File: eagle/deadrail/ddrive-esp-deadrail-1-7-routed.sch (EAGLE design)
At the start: 20 parts, among them Q1 BSS123, Q2 BSS123, Q3 BSS123, Q4 BSS123

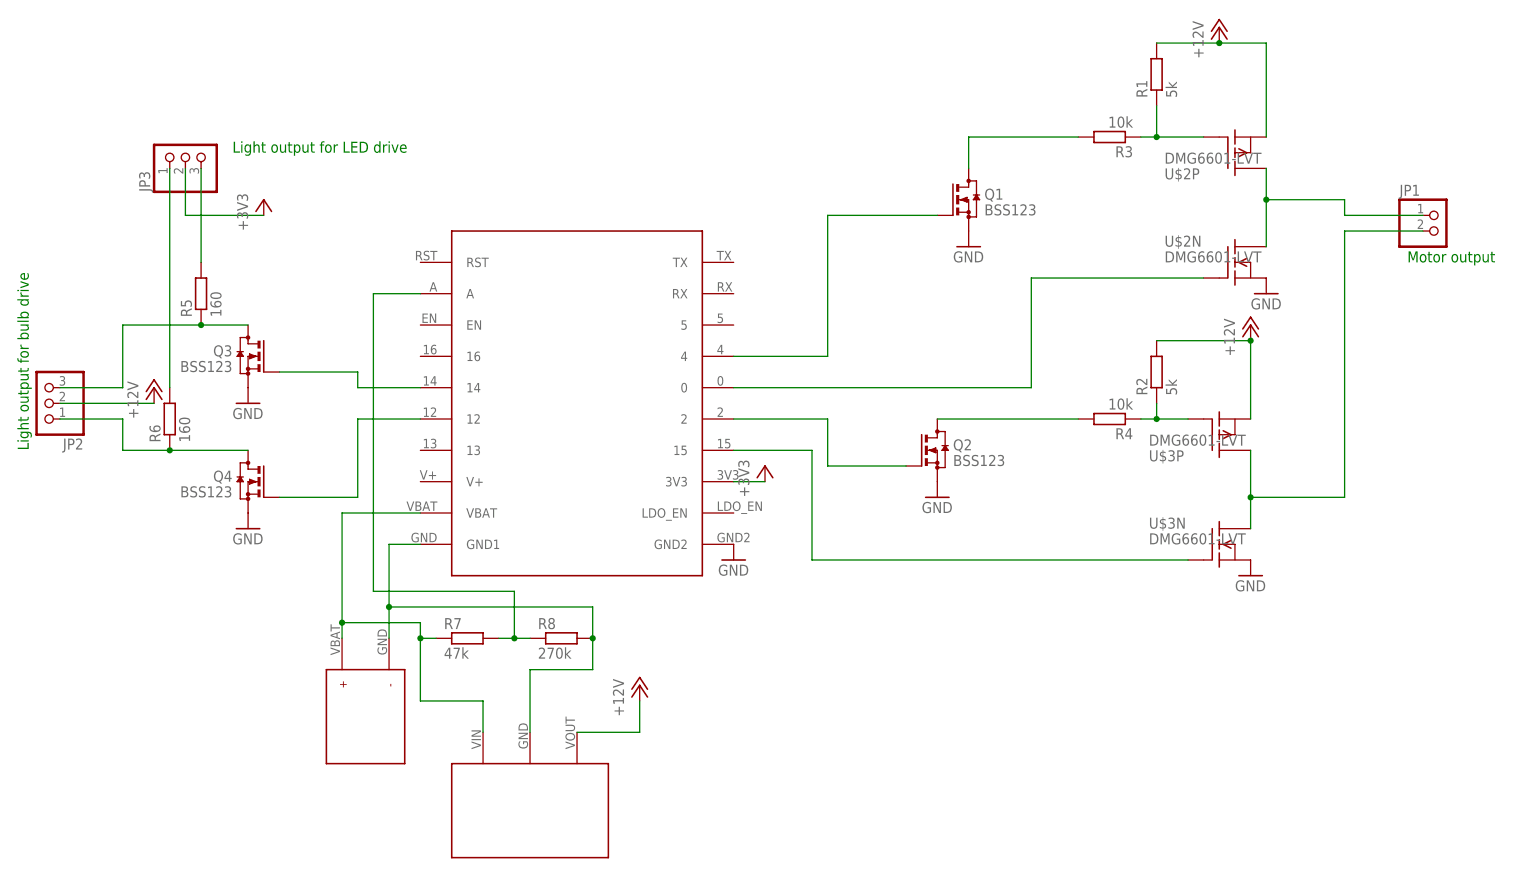
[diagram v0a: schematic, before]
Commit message: Adds all intermediate and the final schematic and board layout for the huzzah baseboard for esp-12 train decoder.
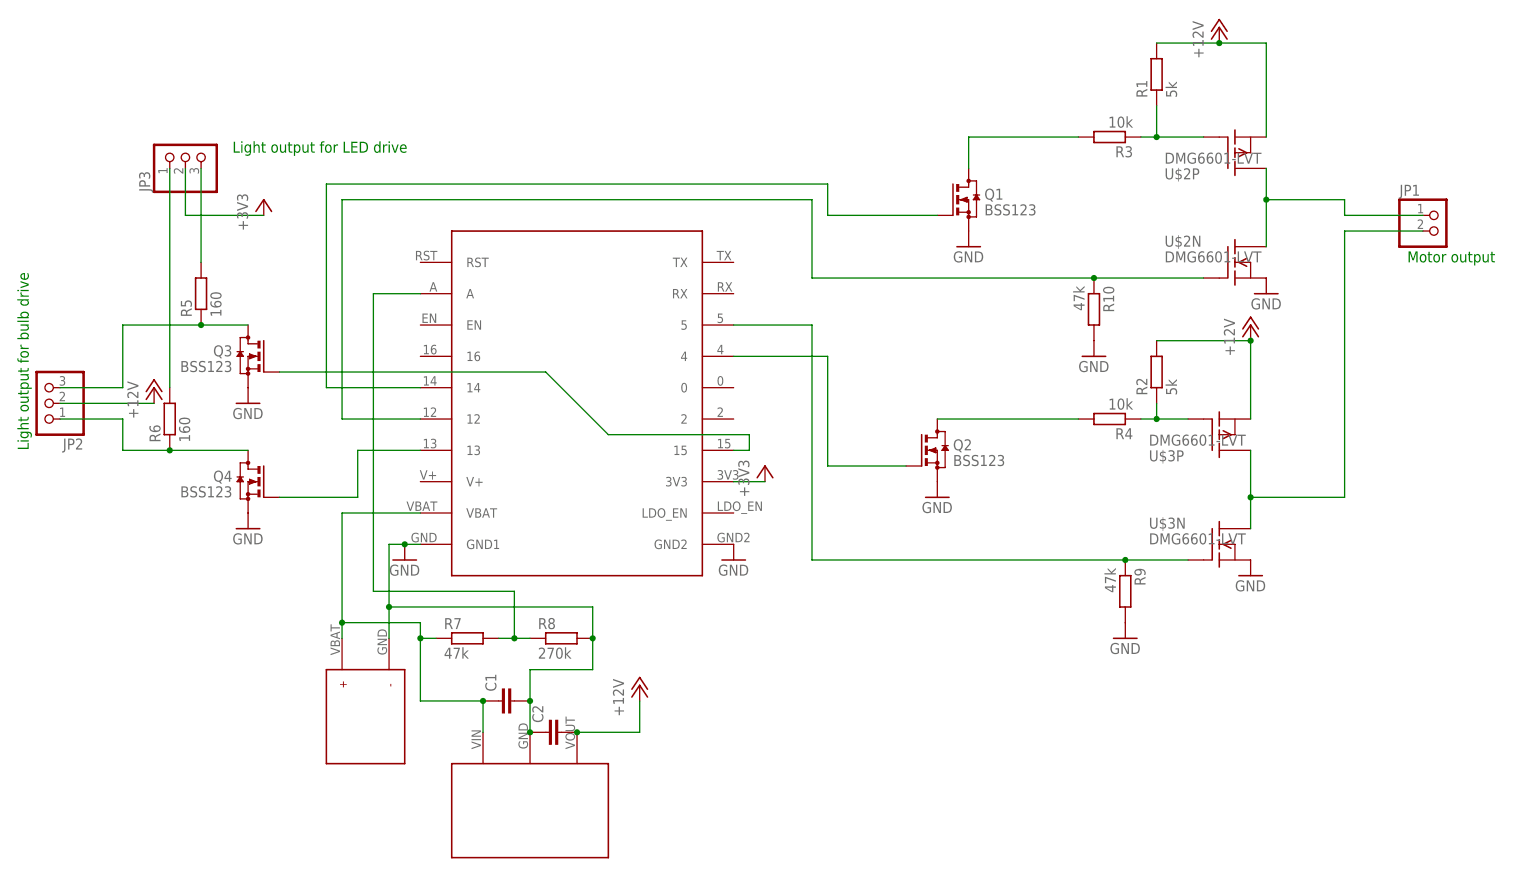
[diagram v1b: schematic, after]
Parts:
- added C1, C2: (no value), rcl:C-EUC1210
- added R10, R9: 47k, rcl:R-EU_R0805
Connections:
- removed net GND1: R8.2, U$1.GND1, U$4.P$1, U$5.GND
- net +12V: now also C2.2
- net GND: now also C1.2, C2.1, R10.2, R8.2, R9.2, U$1.GND1, U$4.P$1, U$5.GND
- net N$10: now also R9.1, U$1.5; no longer U$1.15
- net N$11: now also U$1.15; no longer U$1.14
- net N$12: now also U$1.13; no longer U$1.12
- net N$5: now also U$1.14; no longer U$1.4
- net N$8: now also R10.1, U$1.12; no longer U$1.0
- net N$9: now also U$1.4; no longer U$1.2
- net VBAT: now also C1.1
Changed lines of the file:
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@@
 <part name="U$5" library="trainlib" deviceset="POLOLU-VREG12" device=""/>
 <part name="P+4" library="supply1" deviceset="+12V" device=""/>
+<part name="GND8" library="supply1" deviceset="GND" device=""/>
+<part name="C1" library="rcl" deviceset="C-EU" device="C1210"/>
+<part name="C2" library="rcl" deviceset="C-EU" device="C1210"/>
+<part name="R9" library="rcl" deviceset="R-EU_" device="R0805" value="47k"/>
+<part name="R10" library="rcl" deviceset="R-EU_" device="R0805" value="47k"/>
+<part name="GND9" library="supply1" deviceset="GND" device=""/>
+<part name="GND10" library="supply1" deviceset="GND" device=""/>
 </parts>
 <sheets>
@@
 <instance part="U$5" gate="G$1" x="45.72" y="-22.86" rot="MR180"/>
 <instance part="P+4" gate="1" x="63.5" y="-2.54"/>
+<instance part="GND8" gate="1" x="25.4" y="17.78"/>
+<instance part="C1" gate="G$1" x="40.64" y="-5.08" rot="R90"/>
+<instance part="C2" gate="G$1" x="48.26" y="-10.16" rot="R90"/>
+<instance part="R9" gate="G$1" x="142.24" y="12.7" rot="R270"/>
+<instance part="R10" gate="G$1" x="137.16" y="58.42" rot="R270"/>
+<instance part="GND9" gate="1" x="142.24" y="5.08"/>
+<instance part="GND10" gate="1" x="137.16" y="50.8"/>
 </instances>
 <busses>
@@
 <pinref part="GND7" gate="1" pin="GND"/>
 </segment>
+<segment>
+<pinref part="U$4" gate="G$1" pin="P$1"/>
+<wire x1="22.86" y1="5.08" x2="22.86" y2="10.16" width="0.1524" layer="91"/>
+<pinref part="U$1" gate="G" pin="GND1"/>
+<wire x1="22.86" y1="10.16" x2="22.86" y2="20.32" width="0.1524" layer="91"/>
+<wire x1="22.86" y1="20.32" x2="25.4" y2="20.32" width="0.1524" layer="91"/>
+<pinref part="R8" gate="G$1" pin="2"/>
+<wire x1="25.4" y1="20.32" x2="27.94" y2="20.32" width="0.1524" layer="91"/>
+<wire x1="55.88" y1="5.08" x2="55.88" y2="10.16" width="0.1524" layer="91"/>
+<wire x1="55.88" y1="10.16" x2="22.86" y2="10.16" width="0.1524" layer="91"/>
+<junction x="22.86" y="10.16"/>
+<wire x1="55.88" y1="5.08" x2="55.88" y2="0" width="0.1524" layer="91"/>
+<junction x="55.88" y="5.08"/>
+<pinref part="U$5" gate="G$1" pin="GND"/>
+<wire x1="55.88" y1="0" x2="45.72" y2="0" width="0.1524" layer="91"/>
+<wire x1="45.72" y1="0" x2="45.72" y2="-5.08" width="0.1524" layer="91"/>
+<pinref part="GND8" gate="1" pin="GND"/>
+<junction x="25.4" y="20.32"/>
+<pinref part="C1" gate="G$1" pin="2"/>
+<wire x1="45.72" y1="-5.08" x2="45.72" y2="-10.16" width="0.1524" layer="91"/>
+<junction x="45.72" y="-5.08"/>
+<pinref part="C2" gate="G$1" pin="1"/>
+<junction x="45.72" y="-10.16"/>
+</segment>
+<segment>
+<pinref part="R9" gate="G$1" pin="2"/>
+<pinref part="GND9" gate="1" pin="GND"/>
+</segment>
+<segment>
+<pinref part="R10" gate="G$1" pin="2"/>
+<pinref part="GND10" gate="1" pin="GND"/>
+</segment>
 </net>
 <net name="N$2" class="0">
@@
 <wire x1="63.5" y1="-10.16" x2="63.5" y2="-5.08" width="0.1524" layer="91"/>
 <pinref part="P+4" gate="1" pin="+12V"/>
+<pinref part="C2" gate="G$1" pin="2"/>
+<junction x="53.34" y="-10.16"/>
 </segment>
 </net>
@@
 <pinref part="Q1" gate="G$1" pin="G"/>
 <wire x1="111.76" y1="73.66" x2="93.98" y2="73.66" width="0.1524" layer="91"/>
-<wire x1="93.98" y1="73.66" x2="93.98" y2="50.8" width="0.1524" layer="91"/>
-<pinref part="U$1" gate="G" pin="4"/>
-<wire x1="93.98" y1="50.8" x2="78.74" y2="50.8" width="0.1524" layer="91"/>
+<wire x1="93.98" y1="73.66" x2="93.98" y2="78.74" width="0.1524" layer="91"/>
+<wire x1="93.98" y1="78.74" x2="12.7" y2="78.74" width="0.1524" layer="91"/>
+<wire x1="12.7" y1="78.74" x2="12.7" y2="45.72" width="0.1524" layer="91"/>
+<pinref part="U$1" gate="G" pin="14"/>
+<wire x1="12.7" y1="45.72" x2="27.94" y2="45.72" width="0.1524" layer="91"/>
 </segment>
 </net>
@@
 <segment>
 <pinref part="U$2" gate="N" pin="G"/>
-<wire x1="154.94" y1="63.5" x2="127" y2="63.5" width="0.1524" layer="91"/>
-<wire x1="127" y1="63.5" x2="127" y2="45.72" width="0.1524" layer="91"/>
-<pinref part="U$1" gate="G" pin="0"/>
-<wire x1="127" y1="45.72" x2="78.74" y2="45.72" width="0.1524" layer="91"/>
-</segment>
-</net>
-<net name="N$9" class="0">
-<segment>
-<pinref part="Q2" gate="G$1" pin="G"/>
-<wire x1="106.68" y1="33.02" x2="93.98" y2="33.02" width="0.1524" layer="91"/>
-<wire x1="93.98" y1="33.02" x2="93.98" y2="40.64" width="0.1524" layer="91"/>
-<pinref part="U$1" gate="G" pin="2"/>
-<wire x1="93.98" y1="40.64" x2="78.74" y2="40.64" width="0.1524" layer="91"/>
+<wire x1="154.94" y1="63.5" x2="137.16" y2="63.5" width="0.1524" layer="91"/>
+<wire x1="137.16" y1="63.5" x2="91.44" y2="63.5" width="0.1524" layer="91"/>
+<wire x1="91.44" y1="63.5" x2="91.44" y2="76.2" width="0.1524" layer="91"/>
+<wire x1="91.44" y1="76.2" x2="15.24" y2="76.2" width="0.1524" layer="91"/>
+<wire x1="15.24" y1="76.2" x2="15.24" y2="40.64" width="0.1524" layer="91"/>
+<pinref part="R10" gate="G$1" pin="1"/>
+<junction x="137.16" y="63.5"/>
+<pinref part="U$1" gate="G" pin="12"/>
+<wire x1="15.24" y1="40.64" x2="27.94" y2="40.64" width="0.1524" layer="91"/>
 </segment>
 </net>
@@
 <segment>
 <pinref part="U$3" gate="N" pin="G"/>
-<wire x1="152.4" y1="17.78" x2="91.44" y2="17.78" width="0.1524" layer="91"/>
-<wire x1="91.44" y1="17.78" x2="91.44" y2="35.56" width="0.1524" layer="91"/>
+<wire x1="152.4" y1="17.78" x2="142.24" y2="17.78" width="0.1524" layer="91"/>
+<wire x1="142.24" y1="17.78" x2="91.44" y2="17.78" width="0.1524" layer="91"/>
+<wire x1="91.44" y1="17.78" x2="91.44" y2="55.88" width="0.1524" layer="91"/>
+<pinref part="U$1" gate="G" pin="5"/>
+<wire x1="91.44" y1="55.88" x2="78.74" y2="55.88" width="0.1524" layer="91"/>
+<pinref part="R9" gate="G$1" pin="1"/>
+<junction x="142.24" y="17.78"/>
+</segment>
+</net>
+<net name="N$11" class="0">
+<segment>
+<pinref part="Q3" gate="G$1" pin="G"/>
+<wire x1="5.08" y1="48.26" x2="48.26" y2="48.26" width="0.1524" layer="91"/>
+<wire x1="48.26" y1="48.26" x2="58.42" y2="38.1" width="0.1524" layer="91"/>
+<wire x1="58.42" y1="38.1" x2="81.28" y2="38.1" width="0.1524" layer="91"/>
+<wire x1="81.28" y1="38.1" x2="81.28" y2="35.56" width="0.1524" layer="91"/>
 <pinref part="U$1" gate="G" pin="15"/>
-<wire x1="91.44" y1="35.56" x2="78.74" y2="35.56" width="0.1524" layer="91"/>
-</segment>
-</net>
-<net name="N$11" class="0">
-<segment>
-<pinref part="Q3" gate="G$1" pin="G"/>
-<wire x1="5.08" y1="48.26" x2="17.78" y2="48.26" width="0.1524" layer="91"/>
-<wire x1="17.78" y1="48.26" x2="17.78" y2="45.72" width="0.1524" layer="91"/>
-<pinref part="U$1" gate="G" pin="14"/>
-<wire x1="17.78" y1="45.72" x2="27.94" y2="45.72" width="0.1524" layer="91"/>
+<wire x1="81.28" y1="35.56" x2="78.74" y2="35.56" width="0.1524" layer="91"/>
 </segment>
 </net>
@@
 <pinref part="Q4" gate="G$1" pin="G"/>
 <wire x1="5.08" y1="27.94" x2="17.78" y2="27.94" width="0.1524" layer="91"/>
-<wire x1="17.78" y1="27.94" x2="17.78" y2="40.64" width="0.1524" layer="91"/>
-<pinref part="U$1" gate="G" pin="12"/>
-<wire x1="17.78" y1="40.64" x2="27.94" y2="40.64" width="0.1524" layer="91"/>
+<wire x1="17.78" y1="27.94" x2="17.78" y2="35.56" width="0.1524" layer="91"/>
+<pinref part="U$1" gate="G" pin="13"/>
+<wire x1="17.78" y1="35.56" x2="27.94" y2="35.56" width="0.1524" layer="91"/>
 </segment>
 </net>
@@
 <pinref part="+3V2" gate="G$1" pin="+3V3"/>
 <wire x1="78.74" y1="30.48" x2="83.82" y2="30.48" width="0.1524" layer="91"/>
-</segment>
-</net>
-<net name="GND1" class="0">
-<segment>
-<pinref part="U$4" gate="G$1" pin="P$1"/>
-<wire x1="22.86" y1="5.08" x2="22.86" y2="10.16" width="0.1524" layer="91"/>
-<pinref part="U$1" gate="G" pin="GND1"/>
-<wire x1="22.86" y1="10.16" x2="22.86" y2="20.32" width="0.1524" layer="91"/>
-<wire x1="22.86" y1="20.32" x2="27.94" y2="20.32" width="0.1524" layer="91"/>
-<pinref part="R8" gate="G$1" pin="2"/>
-<wire x1="55.88" y1="5.08" x2="55.88" y2="10.16" width="0.1524" layer="91"/>
-<wire x1="55.88" y1="10.16" x2="22.86" y2="10.16" width="0.1524" layer="91"/>
-<junction x="22.86" y="10.16"/>
-<wire x1="55.88" y1="5.08" x2="55.88" y2="0" width="0.1524" layer="91"/>
-<junction x="55.88" y="5.08"/>
-<pinref part="U$5" gate="G$1" pin="GND"/>
-<wire x1="55.88" y1="0" x2="45.72" y2="0" width="0.1524" layer="91"/>
-<wire x1="45.72" y1="0" x2="45.72" y2="-10.16" width="0.1524" layer="91"/>
 </segment>
 </net>
@@
 <pinref part="U$5" gate="G$1" pin="VIN"/>
 <wire x1="38.1" y1="-5.08" x2="38.1" y2="-10.16" width="0.1524" layer="91"/>
+<pinref part="C1" gate="G$1" pin="1"/>
+<junction x="38.1" y="-5.08"/>
 </segment>
 </net>
@@
 </segment>
 </net>
+<net name="N$9" class="0">
+<segment>
+<pinref part="Q2" gate="G$1" pin="G"/>
+<wire x1="106.68" y1="33.02" x2="93.98" y2="33.02" width="0.1524" layer="91"/>
+<pinref part="U$1" gate="G" pin="4"/>
+<wire x1="93.98" y1="33.02" x2="93.98" y2="50.8" width="0.1524" layer="91"/>
+<wire x1="93.98" y1="50.8" x2="78.74" y2="50.8" width="0.1524" layer="91"/>
+</segment>
+</net>
